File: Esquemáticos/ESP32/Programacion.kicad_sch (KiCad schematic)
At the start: 10 parts, among them U7 ESP32-WROOM-32

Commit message: Algunas huellas añadidas
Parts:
- SW_BOOT1, SW_EN1: footprint (none) -> Button_Switch_SMD:SW_SPST_TL3305A
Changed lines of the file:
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@@
     (property "Reference" "SW_BOOT1" (id 0) (at 226.06 115.57 0))
     (property "Value" "SW_Push" (id 1) (at 226.06 118.11 0))
-    (property "Footprint" "" (id 2) (at 226.06 118.11 0)
+    (property "Footprint" "Button_Switch_SMD:SW_SPST_TL3305A" (id 2) (at 226.06 118.11 0)
       (effects (font (size 1.27 1.27)) hide)
     )
@@
     (property "Reference" "SW_EN1" (id 0) (at 158.75 114.3 0))
     (property "Value" "SW_Push" (id 1) (at 158.75 116.84 0))
-    (property "Footprint" "" (id 2) (at 158.75 116.84 0)
+    (property "Footprint" "Button_Switch_SMD:SW_SPST_TL3305A" (id 2) (at 158.75 116.84 0)
       (effects (font (size 1.27 1.27)) hide)
     )

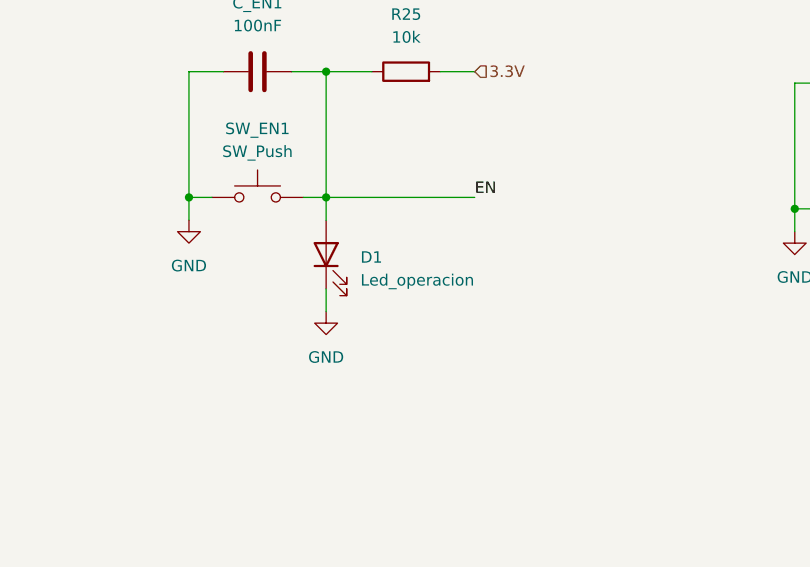
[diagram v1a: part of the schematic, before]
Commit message: me falta el led de programacion
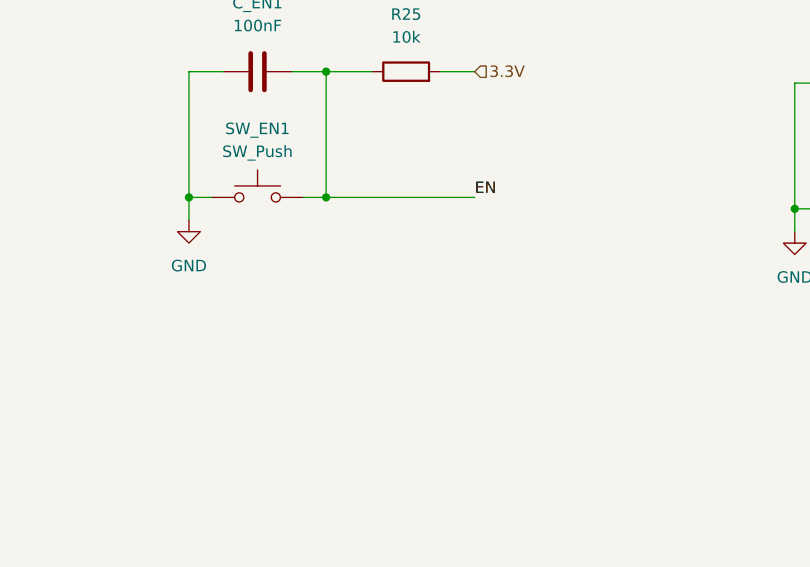
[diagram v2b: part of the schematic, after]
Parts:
- removed D1: Led_operacion, LED_SMD:LED_1206_3216Metric, symbol LED:IR26-21C_L110_TR8
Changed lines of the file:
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@@
-    (stroke (width 0) (type default) (color 0 0 0 0))
-  )
-  (wire (pts (xy 166.37 124.46) (xy 166.37 121.92))
     (stroke (width 0) (type default) (color 0 0 0 0))
   )
@@
   )
   (wire (pts (xy 243.84 123.19) (xy 257.81 123.19))
-    (stroke (width 0) (type default) (color 0 0 0 0))
-  )
-  (wire (pts (xy 166.37 132.08) (xy 166.37 134.62))
     (stroke (width 0) (type default) (color 0 0 0 0))
   )
@@
     )
     (property "Datasheet" "" (id 3) (at 151.13 124.46 0)
-      (effects (font (size 1.27 1.27)) hide)
-    )
-    (pin "1")
-  )
-  (symbol (lib_id "power:GND") (at 166.37 134.62 0) (unit 1)
-    (in_bom yes) (on_board yes) (fields_autoplaced)
-    (property "Reference" "#PWR014" (id 0) (at 166.37 140.97 0)
-      (effects (font (size 1.27 1.27)) hide)
-    )
-    (property "Value" "GND" (id 1) (at 166.37 139.7 0))
-    (property "Footprint" "" (id 2) (at 166.37 134.62 0)
-      (effects (font (size 1.27 1.27)) hide)
-    )
-    (property "Datasheet" "" (id 3) (at 166.37 134.62 0)
       (effects (font (size 1.27 1.27)) hide)
     )
@@
       (effects (font (size 1.27 1.27)) hide)
     )
-    (pin "1")
-    (pin "2")
-  )
-  (symbol (lib_id "LED:IR26-21C_L110_TR8") (at 166.37 128.27 90) (unit 1)
-    (in_bom yes) (on_board yes) (fields_autoplaced)
-    (property "Reference" "D1" (id 0) (at 170.18 128.5874 90)
-      (effects (font (size 1.27 1.27)) (justify right))
-    )
-    (property "Value" "Led_operacion" (id 1) (at 170.18 131.1274 90)
-      (effects (font (size 1.27 1.27)) (justify right))
-    )
-    (property "Footprint" "LED_SMD:LED_1206_3216Metric" (id 2) (at 161.29 128.27 0)
-      (effects (font (size 1.27 1.27)) hide)
-    )
-    (property "Datasheet" "http://www.everlight.com/file/ProductFile/IR26-21C-L110-TR8.pdf" (id 3) (at 166.37 128.27 0)
-      (effects (font (size 1.27 1.27)) hide)
-    )

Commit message: Asignación Huellas de Resistencias
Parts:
- R25, R26, R27: footprint (none) -> Resistor_SMD:R_1206_3216Metric_Pad1.30x1.75mm_HandSolder
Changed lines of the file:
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@@
     (property "Reference" "R26" (id 0) (at 237.49 116.84 90))
     (property "Value" "470" (id 1) (at 237.49 119.38 90))
-    (property "Footprint" "" (id 2) (at 237.49 124.968 90)
+    (property "Footprint" "Resistor_SMD:R_1206_3216Metric_Pad1.30x1.75mm_HandSolder" (id 2) (at 237.49 124.968 90)
       (effects (font (size 1.27 1.27)) hide)
     )
@@
     (property "Reference" "R27" (id 0) (at 250.19 102.87 90))
     (property "Value" "10k" (id 1) (at 250.19 105.41 90))
-    (property "Footprint" "" (id 2) (at 250.19 110.998 90)
+    (property "Footprint" "Resistor_SMD:R_1206_3216Metric_Pad1.30x1.75mm_HandSolder" (id 2) (at 250.19 110.998 90)
       (effects (font (size 1.27 1.27)) hide)
     )
@@
     (property "Reference" "R25" (id 0) (at 175.26 101.6 90))
     (property "Value" "10k" (id 1) (at 175.26 104.14 90))
-    (property "Footprint" "" (id 2) (at 175.26 109.728 90)
+    (property "Footprint" "Resistor_SMD:R_1206_3216Metric_Pad1.30x1.75mm_HandSolder" (id 2) (at 175.26 109.728 90)
       (effects (font (size 1.27 1.27)) hide)
     )

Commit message: lol
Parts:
- added D1: Led_operacion, LED_SMD:LED_1206_3216Metric, symbol LED:IR26-21C_L110_TR8
- R25, R26, R27: footprint Resistor_SMD:R_1206_3216Metric_Pad1.30x1.75mm_HandSolder -> (none)
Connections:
- net EN: now also D1.2 (A)
- net GND: now also D1.1 (K)
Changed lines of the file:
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@@
+    (stroke (width 0) (type default) (color 0 0 0 0))
+  )
+  (wire (pts (xy 166.37 124.46) (xy 166.37 121.92))
     (stroke (width 0) (type default) (color 0 0 0 0))
   )
@@
   )
   (wire (pts (xy 243.84 123.19) (xy 257.81 123.19))
+    (stroke (width 0) (type default) (color 0 0 0 0))
+  )
+  (wire (pts (xy 166.37 132.08) (xy 166.37 134.62))
     (stroke (width 0) (type default) (color 0 0 0 0))
   )
@@
     )
     (property "Datasheet" "" (id 3) (at 151.13 124.46 0)
+      (effects (font (size 1.27 1.27)) hide)
+    )
+    (pin "1")
+  )
+  (symbol (lib_id "power:GND") (at 166.37 134.62 0) (unit 1)
+    (in_bom yes) (on_board yes) (fields_autoplaced)
+    (property "Reference" "#PWR014" (id 0) (at 166.37 140.97 0)
+      (effects (font (size 1.27 1.27)) hide)
+    )
+    (property "Value" "GND" (id 1) (at 166.37 139.7 0))
+    (property "Footprint" "" (id 2) (at 166.37 134.62 0)
+      (effects (font (size 1.27 1.27)) hide)
+    )
+    (property "Datasheet" "" (id 3) (at 166.37 134.62 0)
       (effects (font (size 1.27 1.27)) hide)
     )
@@
     (property "Reference" "R26" (id 0) (at 237.49 116.84 90))
     (property "Value" "470" (id 1) (at 237.49 119.38 90))
-    (property "Footprint" "Resistor_SMD:R_1206_3216Metric_Pad1.30x1.75mm_HandSolder" (id 2) (at 237.49 124.968 90)
+    (property "Footprint" "" (id 2) (at 237.49 124.968 90)
       (effects (font (size 1.27 1.27)) hide)
     )
@@
     (pin "2")
   )
+  (symbol (lib_id "LED:IR26-21C_L110_TR8") (at 166.37 128.27 90) (unit 1)
+    (in_bom yes) (on_board yes) (fields_autoplaced)
+    (property "Reference" "D1" (id 0) (at 170.18 128.5874 90)
+      (effects (font (size 1.27 1.27)) (justify right))
+    )
+    (property "Value" "Led_operacion" (id 1) (at 170.18 131.1274 90)
+      (effects (font (size 1.27 1.27)) (justify right))
+    )
+    (property "Footprint" "LED_SMD:LED_1206_3216Metric" (id 2) (at 161.29 128.27 0)
+      (effects (font (size 1.27 1.27)) hide)
+    )
+    (property "Datasheet" "http://www.everlight.com/file/ProductFile/IR26-21C-L110-TR8.pdf" (id 3) (at 166.37 128.27 0)
+      (effects (font (size 1.27 1.27)) hide)
+    )
+    (pin "1")
+    (pin "2")
+  )
   (symbol (lib_id "Device:R") (at 250.19 109.22 90) (unit 1)
     (in_bom yes) (on_board yes) (fields_autoplaced)
     (property "Reference" "R27" (id 0) (at 250.19 102.87 90))
     (property "Value" "10k" (id 1) (at 250.19 105.41 90))
-    (property "Footprint" "Resistor_SMD:R_1206_3216Metric_Pad1.30x1.75mm_HandSolder" (id 2) (at 250.19 110.998 90)
+    (property "Footprint" "" (id 2) (at 250.19 110.998 90)
       (effects (font (size 1.27 1.27)) hide)
     )
@@
     (property "Reference" "R25" (id 0) (at 175.26 101.6 90))
     (property "Value" "10k" (id 1) (at 175.26 104.14 90))
-    (property "Footprint" "Resistor_SMD:R_1206_3216Metric_Pad1.30x1.75mm_HandSolder" (id 2) (at 175.26 109.728 90)
-      (effects (font (size 1.27 1.27)) hide)
-    )
+    (property "Footprint" "" (id 2) (at 175.26 109.728 90)
+      (effects (font (size 1.27 1.27)) hide)
+    )

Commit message: Eliminando el error de autosave
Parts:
- removed D1: Led_operacion, LED_SMD:LED_1206_3216Metric, symbol LED:IR26-21C_L110_TR8
- R25, R26, R27: footprint (none) -> Resistor_SMD:R_1206_3216Metric_Pad1.30x1.75mm_HandSolder
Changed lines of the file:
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@@
-    (stroke (width 0) (type default) (color 0 0 0 0))
-  )
-  (wire (pts (xy 166.37 124.46) (xy 166.37 121.92))
     (stroke (width 0) (type default) (color 0 0 0 0))
   )
@@
   )
   (wire (pts (xy 243.84 123.19) (xy 257.81 123.19))
-    (stroke (width 0) (type default) (color 0 0 0 0))
-  )
-  (wire (pts (xy 166.37 132.08) (xy 166.37 134.62))
     (stroke (width 0) (type default) (color 0 0 0 0))
   )
@@
     )
     (property "Datasheet" "" (id 3) (at 151.13 124.46 0)
-      (effects (font (size 1.27 1.27)) hide)
-    )
-    (pin "1")
-  )
-  (symbol (lib_id "power:GND") (at 166.37 134.62 0) (unit 1)
-    (in_bom yes) (on_board yes) (fields_autoplaced)
-    (property "Reference" "#PWR014" (id 0) (at 166.37 140.97 0)
-      (effects (font (size 1.27 1.27)) hide)
-    )
-    (property "Value" "GND" (id 1) (at 166.37 139.7 0))
-    (property "Footprint" "" (id 2) (at 166.37 134.62 0)
-      (effects (font (size 1.27 1.27)) hide)
-    )
-    (property "Datasheet" "" (id 3) (at 166.37 134.62 0)
       (effects (font (size 1.27 1.27)) hide)
     )
@@
     (property "Reference" "R26" (id 0) (at 237.49 116.84 90))
     (property "Value" "470" (id 1) (at 237.49 119.38 90))
-    (property "Footprint" "" (id 2) (at 237.49 124.968 90)
+    (property "Footprint" "Resistor_SMD:R_1206_3216Metric_Pad1.30x1.75mm_HandSolder" (id 2) (at 237.49 124.968 90)
       (effects (font (size 1.27 1.27)) hide)
     )
@@
     (pin "2")
   )
-  (symbol (lib_id "LED:IR26-21C_L110_TR8") (at 166.37 128.27 90) (unit 1)
-    (in_bom yes) (on_board yes) (fields_autoplaced)
-    (property "Reference" "D1" (id 0) (at 170.18 128.5874 90)
-      (effects (font (size 1.27 1.27)) (justify right))
-    )
-    (property "Value" "Led_operacion" (id 1) (at 170.18 131.1274 90)
-      (effects (font (size 1.27 1.27)) (justify right))
-    )
-    (property "Footprint" "LED_SMD:LED_1206_3216Metric" (id 2) (at 161.29 128.27 0)
-      (effects (font (size 1.27 1.27)) hide)
-    )
-    (property "Datasheet" "http://www.everlight.com/file/ProductFile/IR26-21C-L110-TR8.pdf" (id 3) (at 166.37 128.27 0)
-      (effects (font (size 1.27 1.27)) hide)
-    )
-    (pin "1")
-    (pin "2")
-  )
   (symbol (lib_id "Device:R") (at 250.19 109.22 90) (unit 1)
     (in_bom yes) (on_board yes) (fields_autoplaced)
     (property "Reference" "R27" (id 0) (at 250.19 102.87 90))
     (property "Value" "10k" (id 1) (at 250.19 105.41 90))
-    (property "Footprint" "" (id 2) (at 250.19 110.998 90)
+    (property "Footprint" "Resistor_SMD:R_1206_3216Metric_Pad1.30x1.75mm_HandSolder" (id 2) (at 250.19 110.998 90)
       (effects (font (size 1.27 1.27)) hide)
     )
@@
     (property "Reference" "R25" (id 0) (at 175.26 101.6 90))
     (property "Value" "10k" (id 1) (at 175.26 104.14 90))
-    (property "Footprint" "" (id 2) (at 175.26 109.728 90)
-      (effects (font (size 1.27 1.27)) hide)
-    )
+    (property "Footprint" "Resistor_SMD:R_1206_3216Metric_Pad1.30x1.75mm_HandSolder" (id 2) (at 175.26 109.728 90)
+      (effects (font (size 1.27 1.27)) hide)
+    )

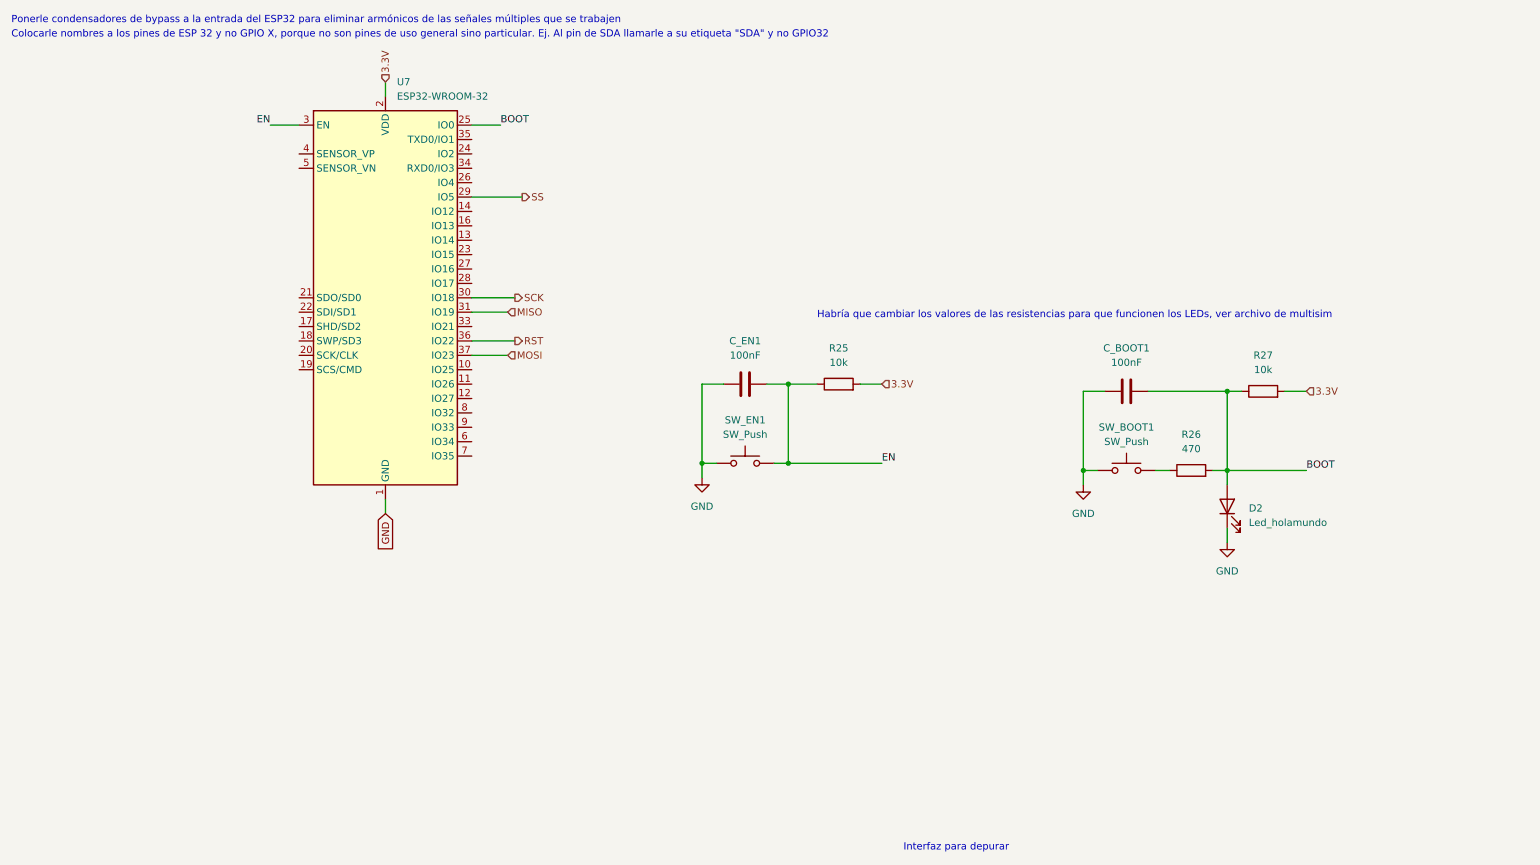
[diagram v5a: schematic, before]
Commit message: Etiquetas globales para alimentación añadidas
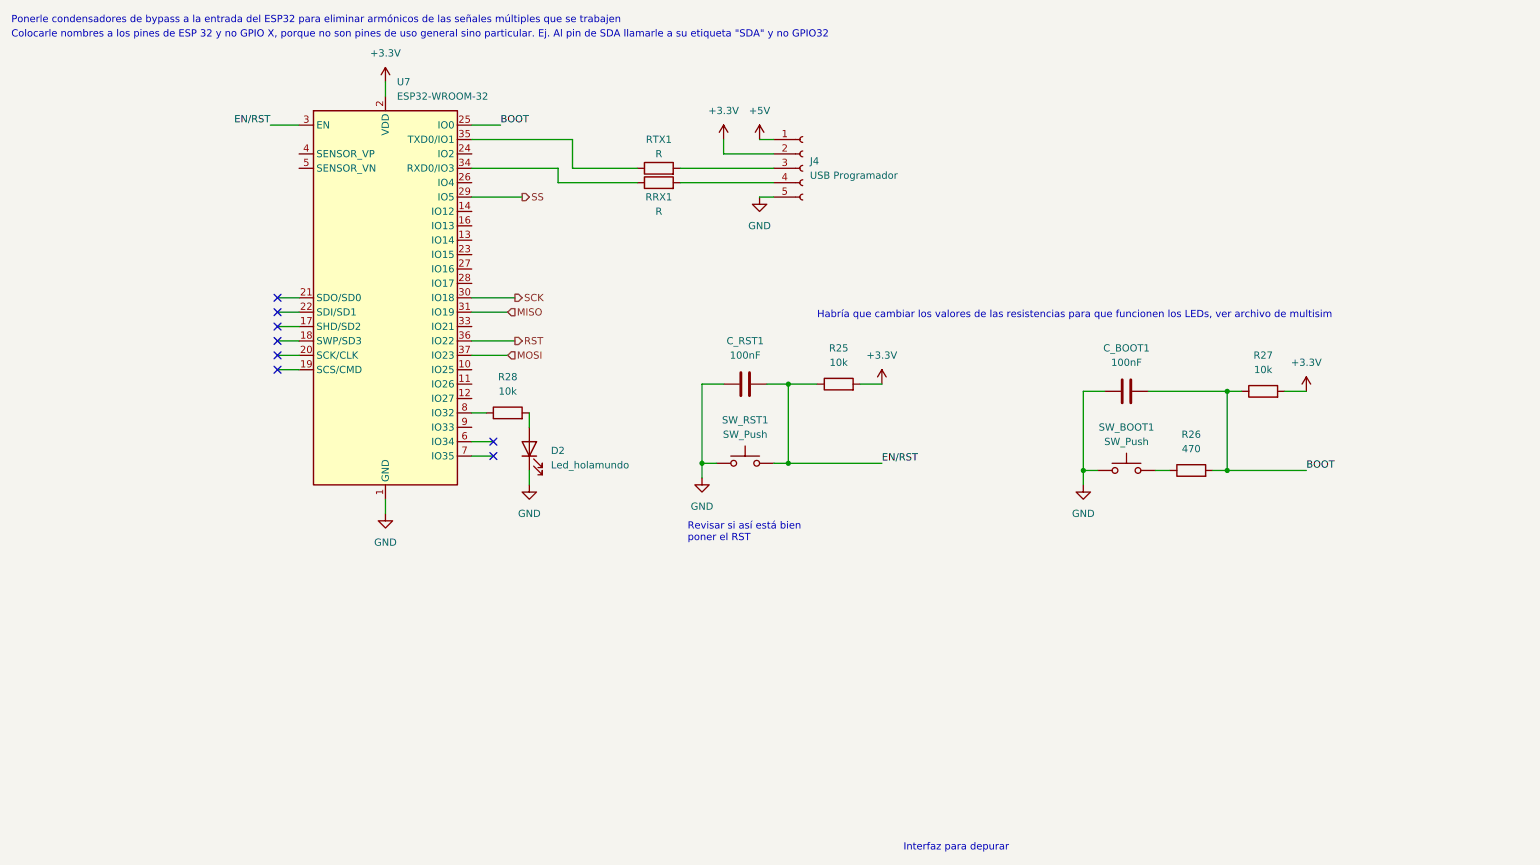
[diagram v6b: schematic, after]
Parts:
- added J4: USB Programador, Connector_PinHeader_1.27mm:PinHeader_1x05_P1.27mm_Vertical, symbol Connector:Conn_01x05_Female
- added R28: 10k, Resistor_SMD:R_1206_3216Metric_Pad1.30x1.75mm_HandSolder, symbol Device:R
- added RRX1, RTX1: R, Resistor_SMD:R_1206_3216Metric_Pad1.30x1.75mm_HandSolder, symbol Device:R
- C_BOOT1: footprint (none) -> Capacitor_SMD:C_0201_0603Metric_Pad0.64x0.40mm_HandSolder
- C_RST1: renamed from C_EN1; footprint (none) -> Capacitor_SMD:C_0201_0603Metric_Pad0.64x0.40mm_HandSolder
- renumbered SW_EN1 to SW_RST1
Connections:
- net BOOT: no longer D2.2 (A)
- net GND: now also J4.5 (Pin_5)
- net at U7.34 (RXD0/IO3): now also RRX1.1
- net at U7.35 (TXD0/IO1): now also RTX1.1
- net at U7.8 (IO32): now also R28.1
- net 3.3V renamed +3.3V
- net +3.3V: now also J4.2 (Pin_2)
- net EN renamed EN/RST
- new net: J4.3 (Pin_3), RTX1.2
- new net: J4.4 (Pin_4), RRX1.2
- new net: D2.2 (A), R28.2
- new net +5V: J4.1 (Pin_1)
- no-connect marks 0 -> 8
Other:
- note added: "Revisar si así está bien poner el RST"

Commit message: añadí leds
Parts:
- R28: value 10k -> 56
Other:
- note removed: "Habría que cambiar los valores de las resistencias para que funcionen los LEDs, ver archivo de multisim"
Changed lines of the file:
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@@
     (stroke (width 0) (type default) (color 0 0 0 0))
-  )
-  (text "Habría que cambiar los valores de las resistencias para que funcionen los LEDs, ver archivo de multisim"
-    (at 171.45 96.52 0)
-    (effects (font (size 1.27 1.27)) (justify left bottom))
   )
   (text "Ponerle condensadores de bypass a la entrada del ESP32 para eliminar armónicos de las señales múltiples que se trabajen\n"
@@
     (in_bom yes) (on_board yes) (fields_autoplaced)
     (property "Reference" "R28" (id 0) (at 116.84 106.68 90))
-    (property "Value" "10k" (id 1) (at 116.84 109.22 90))
+    (property "Value" "56" (id 1) (at 116.84 109.22 90))
     (property "Footprint" "Resistor_SMD:R_1206_3216Metric_Pad1.30x1.75mm_HandSolder" (id 2) (at 116.84 114.808 90)
       (effects (font (size 1.27 1.27)) hide)
